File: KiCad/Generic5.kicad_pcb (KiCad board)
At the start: 2 copper layers, 12.5 x 30 mm, 22 parts, among them J2 Conn_01x04, J3 USB-C, U1 ESP32-PICO-MINI-02, U2 FT231XQ, U3 LMR16006+FB

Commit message: New Generic5
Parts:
- added R7: 27R, RevK:R_0603, B.Cu at (153.5, 39.8)
- added R8: 27R, RevK:R_0603, B.Cu at (154.8, 39.8)
- moved D2 27.4 mm to (152.3, 47.0), turned to -90 degrees
- moved L1 26.0 mm to (155.5, 45.4), turned to -90 degrees
- moved C4 25.0 mm to (151.9, 43.9)
- moved C3 24.9 mm to (151.9, 50.1)
- moved C2 22.0 mm to (155.2, 51.4)
- moved U3 15.6 mm to (155.5, 49.3), turned to 90 degrees
- moved R11 14.7 mm to (149.2, 39.8), turned to 90 degrees
- moved R5 13.6 mm to (150.5, 39.8), turned to 90 degrees
- moved R12 13.6 mm to (149.2, 36.9), turned to 90 degrees
- moved U2 12.2 mm to (154.5, 34.5), turned to 135 degrees
- moved R1 11.5 mm to (158.2, 32.8)
- moved R10 11.3 mm to (158.0, 39.8), turned to -90 degrees
- moved C1 9.73 mm to (158.5, 36.0)
- moved R9 8.73 mm to (159.2, 39.8), turned to -90 degrees
- moved R6 6.73 mm to (156.8, 39.8), turned to -90 degrees
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- renumbered C2 to C1, C5 to C2, C6 to C3, C7 to C4, D3 to D1, D5 to D2, J2 to J1, J3 to J2
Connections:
- J2 pad A6: D+ -> Net-(J2-PadA6)
- J2 pad A7: D- -> Net-(J2-PadA7)
- J2 pad B6: D+ -> Net-(J2-PadA6)
- J2 pad B7: D- -> Net-(J2-PadA7)
- U1 pad 12: R -> unconnected-(U1-Pad12)
- U1 pad 13: G -> unconnected-(U1-Pad13)
- U1 pad 15: B -> unconnected-(U1-Pad15)
- U1 pad 21: IO3 -> unconnected-(U1-Pad21)
- U1 pad 24: IO4 -> B
- U1 pad 26: unconnected-(U1-Pad26) -> G
- U1 pad 27: unconnected-(U1-Pad27) -> IO1
- U1 pad 28: unconnected-(U1-Pad28) -> R
- U1 pad 33: unconnected-(U1-Pad33) -> IO2
- U1 pad 34: IO2 -> IO3
- U1 pad 35: IO1 -> IO4
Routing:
- net +3V3: track 0.00 -> 68.3 mm, vias 0 -> 2
- net GND: track 0.00 -> 57.4 mm, vias 0 -> 7
- net VBUS: track 0.00 -> 50.4 mm, vias 0 -> 1
- net EN: track 0.00 -> 25.4 mm, vias 0 -> 1
- net Net-(R11-Pad2): track 0.00 -> 17.4 mm, vias 0 -> 2
- net B: track 0.00 -> 13.5 mm, vias 0 -> 1
- net Net-(R10-Pad2): track 0.00 -> 13.4 mm
- net Net-(J2-PadA7): track 0.00 -> 11.9 mm, vias 0 -> 2
- net O: track 0.00 -> 10.1 mm, vias 0 -> 1
- net G: track 0.00 -> 10.1 mm, vias 0 -> 1
- net Net-(J2-PadA6): track 0.00 -> 7.04 mm, vias 0 -> 1
- net R: track 0.00 -> 7.01 mm, vias 0 -> 1
- net GPIO0: track 0.00 -> 5.91 mm, vias 0 -> 1
- net Net-(J2-PadA5): track 0.00 -> 5.47 mm, vias 0 -> 1
- net D+: track 0.00 -> 4.53 mm
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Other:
- board size 12.5 x 30 mm -> 12.5 x 31 mm
- board text added: "${DATE}"
- board text added: "www.me.uk"

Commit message: Extra links
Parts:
- added JP1: Jumper_2_Open, RevK:Pad_1206_0805_Open, B.Cu at (157.5, 24.2)
- added JP2: Jumper_2_Open, RevK:Pad_1206_0805_Open, B.Cu at (153.8, 25.6)
- moved R4 2.93 mm to (155.8, 22.6), turned to -90 degrees
- moved R2 1.85 mm to (153.0, 22.4)
- moved R3 0.60 mm to (153.0, 23.6)
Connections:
- U1 pad 26: G -> R
- U1 pad 28: R -> G
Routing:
- net Net-(D1-Pad4): track 1.48 -> 5.32 mm
- net R: track 7.01 -> 10.6 mm
- net B: track 13.5 -> 10.2 mm
- net G: track 10.1 -> 7.47 mm
- net +3V3: track 68.3 -> 70.4 mm
- net IO2: track 4.28 -> 6.37 mm
- net IO1: track 2.36 -> 4.25 mm
- net GND: vias 7 -> 6
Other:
- board text added: "3.3"
- board text added: "GND"

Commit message: Tidy tracks
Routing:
- net GND: track 57.4 -> 55.6 mm
- net +3V3: track 70.4 -> 69.7 mm

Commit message: SIlkscreen
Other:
- board text added: "19"
- board text added: "21"
- board text added: "22"
- board text added: "7"
- board text added: "RGB: 20/8/4"
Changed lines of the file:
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@@
+    (effects (font (size 0.5 0.5) (thickness 0.1)) (justify mirror))
+  )
+  (gr_text "22" (at 152.5 29.1) (layer "B.SilkS")
     (effects (font (size 0.5 0.5) (thickness 0.1)) (justify mirror))
   )
@@
     (effects (font (size 0.5 0.5) (thickness 0.1)) (justify mirror))
   )
-  (gr_text "www.me.uk" (at 154 29.5) (layer "B.SilkS")
+  (gr_text "19" (at 155 29.1) (layer "B.SilkS")
+    (effects (font (size 0.5 0.5) (thickness 0.1)) (justify mirror))
+  )
+  (gr_text "21" (at 150 29.1) (layer "B.SilkS")
+    (effects (font (size 0.5 0.5) (thickness 0.1)) (justify mirror))
+  )
+  (gr_text "RGB: 20/8/4" (at 148.1 21.2 90) (layer "B.SilkS")
+    (effects (font (size 0.5 0.5) (thickness 0.1)) (justify left mirror))
+  )
+  (gr_text "www.me.uk" (at 154 30) (layer "B.SilkS")
     (effects (font (size 1 1) (thickness 0.15)) (justify mirror))
   )
+  (gr_text "7" (at 157.5 29.1) (layer "B.SilkS")
+    (effects (font (size 0.5 0.5) (thickness 0.1)) (justify mirror))
+  )
   (gr_text "www.me.uk" (at 154.25 43.25) (layer "F.SilkS")

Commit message: Tidy
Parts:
- moved R1 0.25 mm to (158.5, 32.8)
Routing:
- net +3V3: track 69.7 -> 63.7 mm
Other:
- board text added: "Generic5"
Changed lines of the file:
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@@
   )
   (footprint "RevK:R_0603" (layer "B.Cu")
-    (at 158.25 32.75 180)
+    (at 158.5 32.75 180)
     (descr "Capacitor SMD 0603 (1608 Metric), square (rectangular) end terminal, IPC_7351 nominal, (Body size source: IPC-SM-782 page 76, https://www.pcb-3d.com/wordpress/wp-content/uploads/ipc-sm-782a_amendment_1_and_2.pdf), generated with kicad-footprint-generator")
     (tags "capacitor")
@@
   (gr_text "RGB: 20/8/4" (at 148.1 21.2 90) (layer "B.SilkS")
     (effects (font (size 0.5 0.5) (thickness 0.1)) (justify left mirror))
+  )
+  (gr_text "Generic5" (at 150.5 34.5 90) (layer "B.SilkS")
+    (effects (font (size 0.75 0.75) (thickness 0.1)) (justify mirror))
   )
   (gr_text "www.me.uk" (at 154 30) (layer "B.SilkS")
@@
   (arc (start 151.589696 40.5) (mid 150.642388 40.107612) (end 150.25 39.160304) (width 0.25) (layer "F.Cu") (net 3))
   (segment (start 152.6 39.4) (end 152.6 39.265685) (width 0.25) (layer "B.Cu") (net 3))
+  (segment (start 157.525499 30.525499) (end 157.525499 30.865329) (width 0.25) (layer "B.Cu") (net 3))
   (segment (start 152.094975 38.194974) (end 152.2 38.3) (width 0.25) (layer "B.Cu") (net 3))
-  (segment (start 159.075 32.75) (end 159.275 32.95) (width 0.25) (layer "B.Cu") (net 3))
   (segment (start 152 40.5) (end 152.246447 40.253554) (width 0.25) (layer "B.Cu") (net 3))
+  (segment (start 159.325 32.75) (end 159.325 35.87929) (width 0.25) (layer "B.Cu") (net 3))
   (segment (start 152.44939 33.863604) (end 152.44939 35.136396) (width 0.25) (layer "B.Cu") (net 3))
   (segment (start 152 40.5) (end 152 43) (width 0.25) (layer "B.Cu") (net 3))
-  (segment (start 159.275 32.95) (end 159.275 36) (width 0.25) (layer "B.Cu") (net 3))
-  (segment (start 157.7625 31.4375) (end 159.075 32.75) (width 0.25) (layer "B.Cu") (net 3))
   (segment (start 152.44939 33.863604) (end 152.449391 33.863604) (width 0.25) (layer "B.Cu") (net 3))
-  (segment (start 151.25 29.5) (end 157 29.5) (width 0.25) (layer "B.Cu") (net 3))
+  (segment (start 151.25 29.5) (end 156.5 29.5) (width 0.25) (layer "B.Cu") (net 3))
   (segment (start 149.6 24.6) (end 151.2875 24.6) (width 0.25) (layer "B.Cu") (net 3))
+  (segment (start 159.275 36) (end 159.275 38.864645) (width 0.25) (layer "B.Cu") (net 3))
   (segment (start 151.896447 32.603556) (end 152.802944 33.510051) (width 0.25) (layer "B.Cu") (net 3))
-  (segment (start 159.25 34) (end 159.25 32.925) (width 0.25) (layer "B.Cu") (net 3))
   (segment (start 159.25 34) (end 156.879899 34) (width 0.25) (layer "B.Cu") (net 3))
-  (segment (start 159.25 38.925) (end 159.25 34) (width 0.25) (layer "B.Cu") (net 3))
+  (segment (start 157.7625 31.4375) (end 159.275 32.95) (width 0.25) (layer "B.Cu") (net 3))
   (segment (start 150 30.75) (end 150 31.3) (width 0.25) (layer "B.Cu") (net 3))
   (segment (start 151.25 26.6375) (end 151.25 29.5) (width 0.25) (layer "B.Cu") (net 3))
   (segment (start 152.449391 33.863604) (end 152.802944 33.510051) (width 0.25) (layer "B.Cu") (net 3))
   (segment (start 151.75 32) (end 151.75 32.25) (width 0.25) (layer "B.Cu") (net 3))
-  (segment (start 157.525499 30.025499) (end 157.525499 30.865329) (width 0.25) (layer "B.Cu") (net 3))
   (segment (start 150.95 32.25) (end 151.75 32.25) (width 0.25) (layer "B.Cu") (net 3))
   (segment (start 149.136022 22.488978) (end 149.136022 24.136022) (width 0.25) (layer "B.Cu") (net 3))
   (segment (start 152.44939 35.136396) (end 152.317158 35.268628) (width 0.25) (layer "B.Cu") (net 3))
   (segment (start 159.275 38.9) (end 159.25 38.925) (width 0.25) (layer "B.Cu") (net 3))
-  (segment (start 159.275 36) (end 159.275 38.9) (width 0.25) (layer "B.Cu") (net 3))
   (arc (start 152 43) (mid 152.263604 43.636396) (end 152.9 43.9) (width 0.25) (layer "B.Cu") (net 3))
   (arc (start 149.136022 24.136022) (mid 149.271918 24.464104) (end 149.6 24.6) (width 0.25) (layer "B.Cu") (net 3))
+  (arc (start 157.525499 30.865329) (mid 157.587094 31.174985) (end 157.7625 31.4375) (width 0.25) (layer "B.Cu") (net 3))
   (arc (start 152.317158 35.268628) (mid 151.786383 36.062988) (end 151.6 37) (width 0.25) (layer "B.Cu") (net 3))
   (arc (start 149.75 21.875) (mid 149.315852 22.05483) (end 149.136022 22.488978) (width 0.25) (layer "B.Cu") (net 3))
+  (arc (start 156.5 29.5) (mid 157.225137 29.800362) (end 157.525499 30.525499) (width 0.25) (layer "B.Cu") (net 3))
   (arc (start 151.75 32.25) (mid 151.78806 32.441343) (end 151.896447 32.603556) (width 0.25) (layer "B.Cu") (net 3))
   (arc (start 151.2875 24.6) (mid 151.994607 24.892893) (end 152.2875 25.6) (width 0.25) (layer "B.Cu") (net 3))
@@
   (arc (start 151.6 37) (mid 151.72864 37.646715) (end 152.094975 38.194974) (width 0.25) (layer "B.Cu") (net 3))
   (arc (start 156.879899 34) (mid 156.701689 33.964552) (end 156.55061 33.863604) (width 0.25) (layer "B.Cu") (net 3))
-  (arc (start 157.525499 30.865329) (mid 157.587094 31.174985) (end 157.7625 31.4375) (width 0.25) (layer "B.Cu") (net 3))
   (arc (start 151.25 29.5) (mid 150.366117 29.866117) (end 150 30.75) (width 0.25) (layer "B.Cu") (net 3))
+  (arc (start 159.275 38.864645) (mid 159.268502 38.897309) (end 159.25 38.925) (width 0.25) (layer "B.Cu") (net 3))
   (arc (start 150 31.3) (mid 150.278249 31.971751) (end 150.95 32.25) (width 0.25) (layer "B.Cu") (net 3))
   (arc (start 152.5 31.25) (mid 151.96967 31.46967) (end 151.75 32) (width 0.25) (layer "B.Cu") (net 3))
+  (arc (start 159.325 35.87929) (mid 159.312005 35.944618) (end 159.275 36) (width 0.25) (layer "B.Cu") (net 3))
   (arc (start 152.2875 25.6) (mid 151.553877 25.903877) (end 151.25 26.6375) (width 0.25) (layer "B.Cu") (net 3))
   (arc (start 152.6 39.265685) (mid 152.496043 38.74306) (end 152.2 38.3) (width 0.25) (layer "B.Cu") (net 3))
-  (arc (start 157 29.5) (mid 157.371584 29.653915) (end 157.525499 30.025499) (width 0.25) (layer "B.Cu") (net 3))
   (segment (start 151.95 29.65) (end 151.95 29.150978) (width 0.25) (layer "F.Cu") (net 4))
   (segment (start 152.175489 28.925489) (end 153.674511 28.925489) (width 0.25) (layer "F.Cu") (net 4))
@@
   (via (at 158.25 30.75) (size 0.8) (drill 0.4) (layers "F.Cu" "B.Cu") (net 16))
   (segment (start 156.30048 23.92548) (end 156.30048 28.20048) (width 0.25) (layer "B.Cu") (net 16))
-  (segment (start 157.1 29) (end 157.3 29) (width 0.25) (layer "B.Cu") (net 16))
-  (segment (start 158.25 30.75) (end 158.25 29.95) (width 0.25) (layer "B.Cu") (net 16))
+  (segment (start 158.25 30.15) (end 158.25 30.75) (width 0.25) (layer "B.Cu") (net 16))
   (arc (start 156.30048 28.20048) (mid 156.534654 28.765826) (end 157.1 29) (width 0.25) (layer "B.Cu") (net 16))
   (arc (start 155.8 23.425) (mid 156.153893 23.571587) (end 156.30048 23.92548) (width 0.25) (layer "B.Cu") (net 16))
-  (arc (start 158.25 29.95) (mid 157.971751 29.278249) (end 157.3 29) (width 0.25) (layer "B.Cu") (net 16))
+  (arc (start 157.1 29) (mid 157.913173 29.336827) (end 158.25 30.15) (width 0.25) (layer "B.Cu") (net 16))
   (segment (start 152.802944 35.489949) (end 152.564865 35.728028) (width 0.25) (layer "B.Cu") (net 17))
   (segment (start 152.627388 38.052389) (end 153.5 38.925) (width 0.25) (layer "B.Cu") (net 17))
@@
   (arc (start 154.524501 39.724501) (mid 155.532481 40.14202) (end 155.95 41.15) (width 0.25) (layer "F.Cu") (net 21))
   (arc (start 150.775499 31.499099) (mid 150.844856 31.331656) (end 151.012299 31.262299) (width 0.25) (layer "F.Cu") (net 21))
-  (segment (start 157.075989 30.211693) (end 157.075989 32.400989) (width 0.25) (layer "B.Cu") (net 21))
+  (segment (start 157.424998 32.75) (end 157.675 32.75) (width 0.25) (layer "B.Cu") (net 21))
   (segment (start 156.626256 33.08085) (end 156.197056 33.510051) (width 0.25) (layer "B.Cu") (net 21))
-  (segment (start 152.325087 29.949511) (end 156.813807 29.949511) (width 0.25) (layer "B.Cu") (net 21))
+  (segment (start 157.075989 31.174011) (end 157.075989 31.30386) (width 0.25) (layer "B.Cu") (net 21))
+  (segment (start 157.075989 30.725011) (end 157.075989 31.174011) (width 0.25) (layer "B.Cu") (net 21))
+  (segment (start 152.325087 29.949511) (end 156.300489 29.949511) (width 0.25) (layer "B.Cu") (net 21))
+  (arc (start 157.075989 31.30386) (mid 157.231667 32.086505) (end 157.675 32.75) (width 0.25) (layer "B.Cu") (net 21))
+  (arc (start 156.626256 33.08085) (mid 156.992722 32.835985) (end 157.424998 32.75) (width 0.25) (layer "B.Cu") (net 21))
+  (arc (start 156.300489 29.949511) (mid 156.84885 30.17665) (end 157.075989 30.725011) (width 0.25) (layer "B.Cu") (net 21))
   (arc (start 151.012299 31.262299) (mid 151.396806 30.334018) (end 152.325087 29.949511) (width 0.25) (layer "B.Cu") (net 21))
-  (arc (start 157.425 32.75) (mid 156.992723 32.835985) (end 156.626256 33.08085) (width 0.25) (layer "B.Cu") (net 21))
-  (arc (start 157.075989 32.400989) (mid 157.178212 32.647777) (end 157.425 32.75) (width 0.25) (layer "B.Cu") (net 21))
-  (arc (start 156.813807 29.949511) (mid 156.999198 30.026302) (end 157.075989 30.211693) (width 0.25) (layer "B.Cu") (net 21))
   (segment (start 157.05 31.55) (end 159.25 31.55) (width 0.25) (layer "F.Cu") (net 24))
   (via (at 156.25 30.75) (size 0.8) (drill 0.4) (layers "F.Cu" "B.Cu") (net 24))

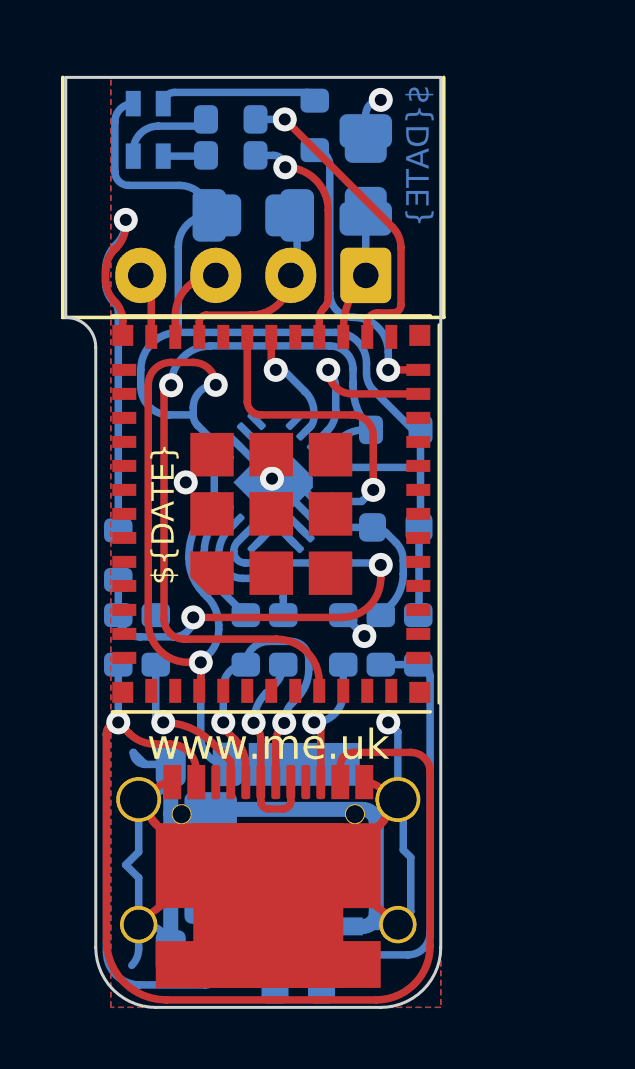
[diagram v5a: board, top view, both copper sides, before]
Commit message: New 5V link
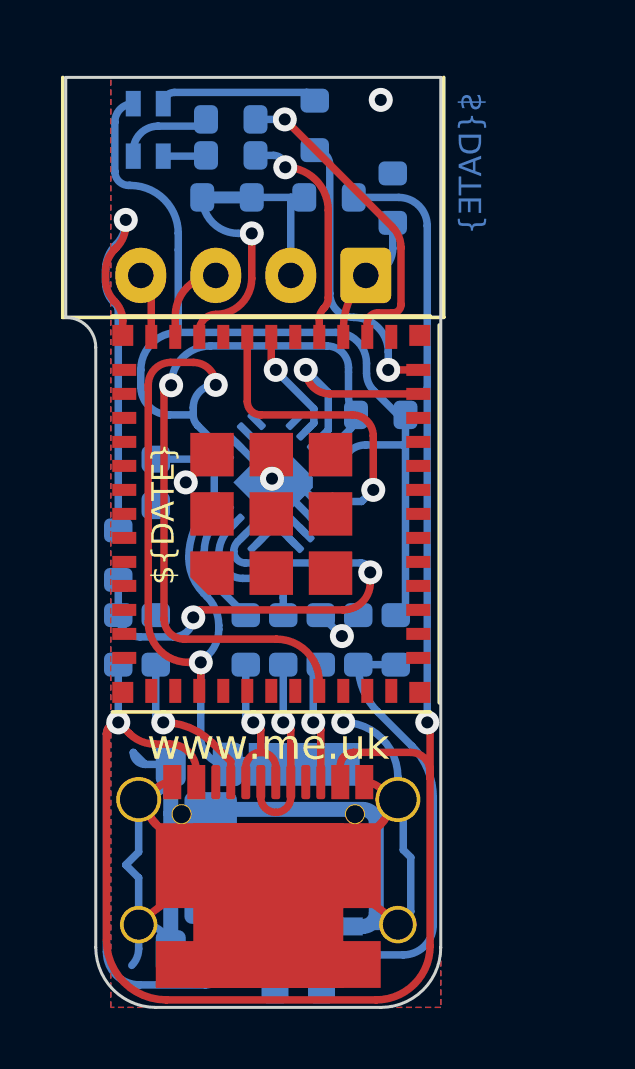
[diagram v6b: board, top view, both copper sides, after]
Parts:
- added JP3: Jumper_2_Bridged, RevK:Pad_0603_Bridged, B.Cu at (152.9, 25.0)
- JP1, JP2: footprint RevK:Pad_1206_0805_Open -> RevK:Pad_0603_Open
- moved C1 8.14 mm to (150.5, 34.5), turned to -90 degrees
- moved JP2 2.62 mm to (156.3, 25.0), turned to 180 degrees
- moved JP1 1.17 mm to (158.4, 25.0)
- moved R10 0.75 mm to (157.2, 39.8)
- moved R6 0.75 mm to (156.0, 39.8)
- moved R9 0.75 mm to (158.5, 39.8)
- moved R1 0.71 mm to (158.0, 32.2)
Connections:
- J1 pad 2: IO2 -> Net-(J1-Pad2)
- JP2 pad 1: +3V3 -> VBUS
- JP2 pad 2: IO2 -> Net-(J1-Pad2)
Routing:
- net VBUS: track 50.0 -> 71.4 mm, vias 1 -> 2
- net Net-(J2-PadA7): track 11.8 -> 5.70 mm, vias 2 -> 1
- net GND: track 55.6 -> 49.7 mm
- net Net-(J1-Pad2): track 0.00 -> 4.38 mm
- net GPIO0: track 6.12 -> 7.06 mm
- net EN: track 25.6 -> 24.8 mm
- net Net-(R11-Pad2): track 17.7 -> 16.9 mm
- net Net-(R10-Pad2): track 13.6 -> 14.2 mm
- net IO2: track 6.43 -> 6.67 mm, vias 0 -> 1
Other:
- board text added: "5V"
- board text added: "⏚"
- board text removed: "3.3"
- board text removed: "GND"

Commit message: Ready for order
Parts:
- added Logo1: AJK, RevK:AJK, F.Cu at (151.8, 24.2)
- moved JP3 0.85 mm to (153.8, 25.0)
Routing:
- net GND: track 49.7 -> 46.6 mm, vias 6 -> 7
- net R: track 10.6 -> 11.6 mm
- net Net-(J1-Pad2): track 4.38 -> 3.50 mm
- net O: track 10.1 -> 9.37 mm
